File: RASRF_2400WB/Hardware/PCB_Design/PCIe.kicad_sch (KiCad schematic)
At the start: 1 part, among them J1 PCIexpress_x8

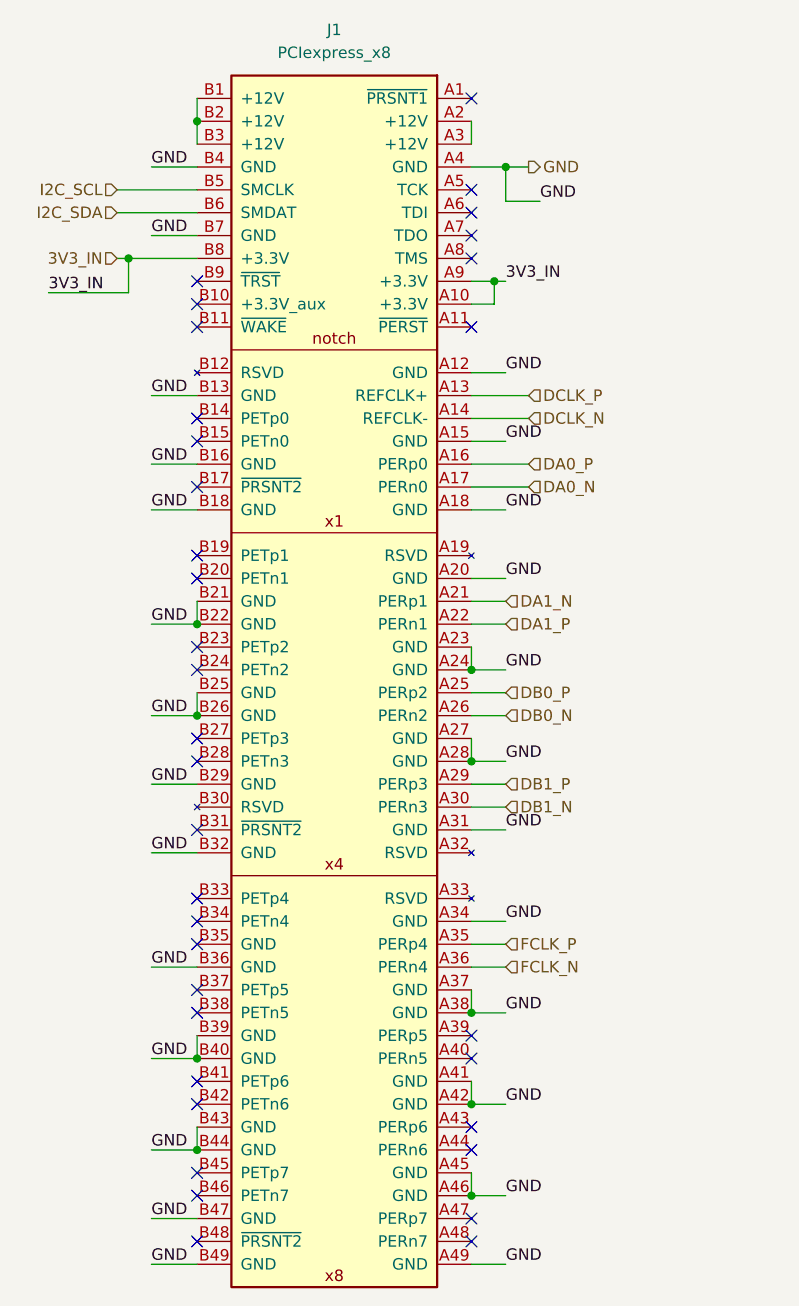
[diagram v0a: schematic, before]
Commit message: Corrected the RASRF_2400WB PCB design files. They where not the latest from Rev. A. sent to manufacturer.
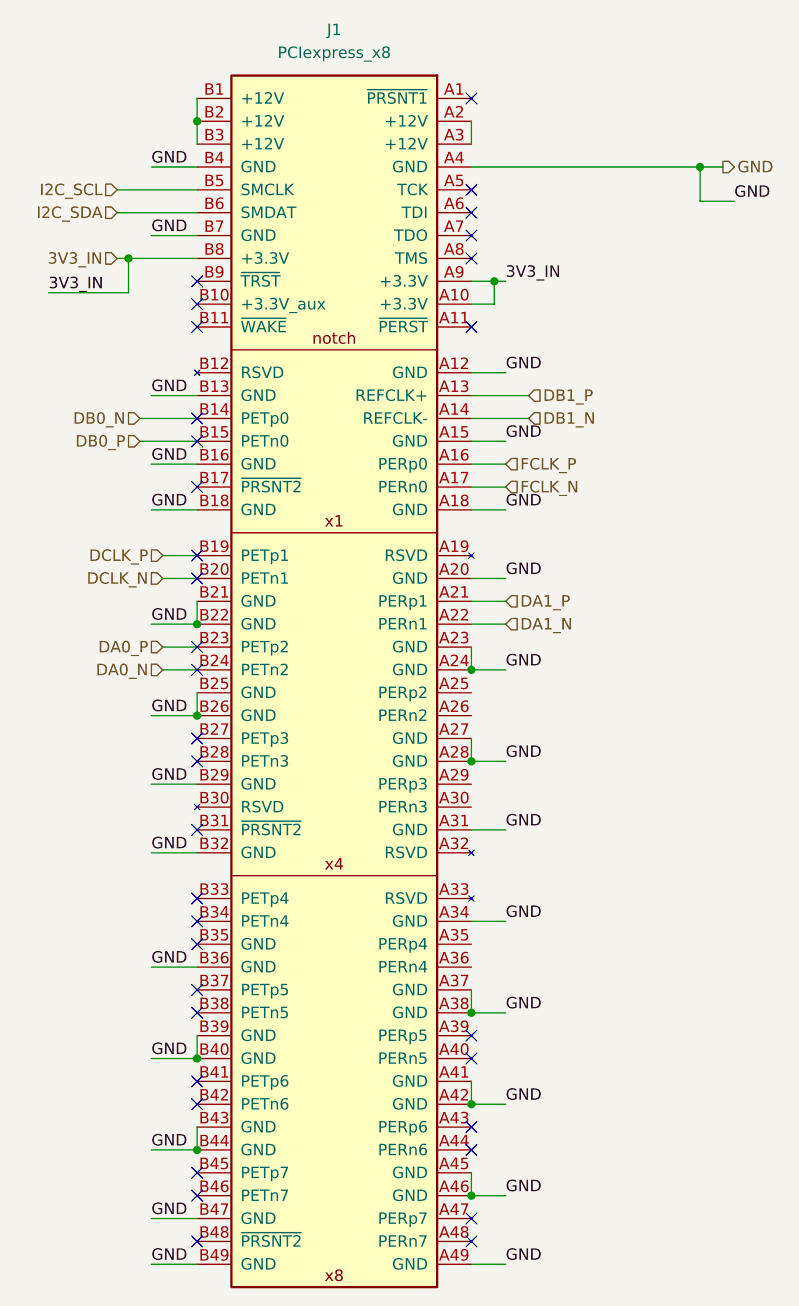
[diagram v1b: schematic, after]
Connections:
- net DA0_N: now also J1.B24 (PETn2); no longer J1.A17 (PERn0)
- net DA0_P: now also J1.B23 (PETp2); no longer J1.A16 (PERp0)
- net DA1_N: now also J1.A22 (PERn1); no longer J1.A21 (PERp1)
- net DA1_P: now also J1.A21 (PERp1); no longer J1.A22 (PERn1)
- net DB0_N: now also J1.B14 (PETp0); no longer J1.A26 (PERn2)
- net DB0_P: now also J1.B15 (PETn0); no longer J1.A25 (PERp2)
- net DB1_N: now also J1.A14 (REFCLK-); no longer J1.A30 (PERn3)
- net DB1_P: now also J1.A13 (REFCLK+); no longer J1.A29 (PERp3)
- net DCLK_N: now also J1.B20 (PETn1); no longer J1.A14 (REFCLK-)
- net DCLK_P: now also J1.B19 (PETp1); no longer J1.A13 (REFCLK+)
- net FCLK_N: now also J1.A17 (PERn0); no longer J1.A36 (PERn4)
- net FCLK_P: now also J1.A16 (PERp0); no longer J1.A35 (PERp4)
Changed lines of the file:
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@@
 	)
 	(junction
-		(at 106.68 45.72)
+		(at 128.27 45.72)
 		(diameter 0)
 		(color 0 0 0 0)
@@
 	(wire
 		(pts
-			(xy 106.68 134.62) (xy 102.87 134.62)
-		)
-		(stroke
-			(width 0)
-			(type default)
-		)
-	)
-	(wire
-		(pts
-			(xy 106.68 114.3) (xy 102.87 114.3)
+			(xy 102.87 45.72) (xy 128.27 45.72)
 		)
 		(stroke
@@
 	(wire
 		(pts
-			(xy 102.87 81.28) (xy 109.22 81.28)
-		)
-		(stroke
-			(width 0)
-			(type default)
-		)
-	)
-	(wire
-		(pts
 			(xy 67.31 71.12) (xy 72.39 71.12)
 		)
@@
 	(wire
 		(pts
-			(xy 110.49 49.53) (xy 106.68 49.53)
-		)
-		(stroke
-			(width 0)
-			(type default)
-		)
-	)
-	(wire
-		(pts
-			(xy 106.68 49.53) (xy 106.68 45.72)
+			(xy 132.08 49.53) (xy 128.27 49.53)
+		)
+		(stroke
+			(width 0)
+			(type default)
+		)
+	)
+	(wire
+		(pts
+			(xy 128.27 49.53) (xy 128.27 45.72)
 		)
 		(stroke
@@
 	(wire
 		(pts
-			(xy 106.68 132.08) (xy 102.87 132.08)
+			(xy 106.68 81.28) (xy 102.87 81.28)
 		)
 		(stroke
@@
 	(wire
 		(pts
+			(xy 68.58 91.44) (xy 72.39 91.44)
+		)
+		(stroke
+			(width 0)
+			(type default)
+		)
+	)
+	(wire
+		(pts
 			(xy 102.87 149.86) (xy 106.68 149.86)
 		)
@@
 	(wire
 		(pts
-			(xy 106.68 104.14) (xy 102.87 104.14)
+			(xy 68.58 88.9) (xy 72.39 88.9)
 		)
 		(stroke
@@
 	(wire
 		(pts
+			(xy 68.58 99.06) (xy 72.39 99.06)
+		)
+		(stroke
+			(width 0)
+			(type default)
+		)
+	)
+	(wire
+		(pts
 			(xy 102.87 157.48) (xy 102.87 160.02)
 		)
@@
 	(wire
 		(pts
+			(xy 106.68 78.74) (xy 102.87 78.74)
+		)
+		(stroke
+			(width 0)
+			(type default)
+		)
+	)
+	(wire
+		(pts
 			(xy 102.87 76.2) (xy 106.68 76.2)
 		)
@@
 	(wire
 		(pts
+			(xy 72.39 76.2) (xy 66.04 76.2)
+		)
+		(stroke
+			(width 0)
+			(type default)
+		)
+	)
+	(wire
+		(pts
+			(xy 68.58 101.6) (xy 72.39 101.6)
+		)
+		(stroke
+			(width 0)
+			(type default)
+		)
+	)
+	(wire
+		(pts
 			(xy 109.22 73.66) (xy 102.87 73.66)
 		)
@@
 	(wire
 		(pts
-			(xy 106.68 106.68) (xy 102.87 106.68)
-		)
-		(stroke
-			(width 0)
-			(type default)
-		)
-	)
-	(wire
-		(pts
 			(xy 67.31 162.56) (xy 72.39 162.56)
 		)
@@
 	(wire
 		(pts
-			(xy 106.68 116.84) (xy 102.87 116.84)
-		)
-		(stroke
-			(width 0)
-			(type default)
-		)
-	)
-	(wire
-		(pts
-			(xy 102.87 78.74) (xy 109.22 78.74)
-		)
-		(stroke
-			(width 0)
-			(type default)
-		)
-	)
-	(wire
-		(pts
 			(xy 102.87 71.12) (xy 109.22 71.12)
 		)
@@
 	(wire
 		(pts
+			(xy 72.39 73.66) (xy 66.04 73.66)
+		)
+		(stroke
+			(width 0)
+			(type default)
+		)
+	)
+	(wire
+		(pts
 			(xy 106.68 93.98) (xy 102.87 93.98)
 		)
@@
 	(wire
 		(pts
-			(xy 109.22 45.72) (xy 106.68 45.72)
+			(xy 130.81 45.72) (xy 128.27 45.72)
 		)
 		(stroke
@@
 		(pts
 			(xy 67.31 114.3) (xy 72.39 114.3)
-		)
-		(stroke
-			(width 0)
-			(type default)
-		)
-	)
-	(wire
-		(pts
-			(xy 106.68 45.72) (xy 102.87 45.72)
 		)
 		(stroke
@@
 	)
 	(label "GND"
-		(at 110.49 49.53 0)
+		(at 132.08 49.53 0)
 		(effects
 			(font
@@
 		)
 	)
+	(hierarchical_label "DA1_P"
+		(shape input)
+		(at 106.68 93.98 0)
+		(effects
+			(font
+				(size 1.27 1.27)
+			)
+			(justify left)
+		)
+	)
+	(hierarchical_label "DB0_P"
+		(shape input)
+		(at 66.04 76.2 180)
+		(effects
+			(font
+				(size 1.27 1.27)
+			)
+			(justify right)
+		)
+	)
+	(hierarchical_label "DB1_P"
+		(shape input)
+		(at 109.22 71.12 0)
+		(effects
+			(font
+				(size 1.27 1.27)
+			)
+			(justify left)
+		)
+	)
+	(hierarchical_label "FCLK_N"
+		(shape input)
+		(at 106.68 81.28 0)
+		(effects
+			(font
+				(size 1.27 1.27)
+			)
+			(justify left)
+		)
+	)
+	(hierarchical_label "FCLK_P"
+		(shape input)
+		(at 106.68 78.74 0)
+		(effects
+			(font
+				(size 1.27 1.27)
+			)
+			(justify left)
+		)
+	)
 	(hierarchical_label "DA1_N"
-		(shape input)
-		(at 106.68 93.98 0)
-		(effects
-			(font
-				(size 1.27 1.27)
-			)
-			(justify left)
-		)
-	)
-	(hierarchical_label "FCLK_P"
-		(shape input)
-		(at 106.68 132.08 0)
-		(effects
-			(font
-				(size 1.27 1.27)
-			)
-			(justify left)
-		)
-	)
-	(hierarchical_label "DB0_N"
-		(shape input)
-		(at 106.68 106.68 0)
-		(effects
-			(font
-				(size 1.27 1.27)
-			)
-			(justify left)
-		)
-	)
-	(hierarchical_label "DCLK_P"
-		(shape input)
-		(at 109.22 71.12 0)
-		(effects
-			(font
-				(size 1.27 1.27)
-			)
-			(justify left)
-		)
-	)
-	(hierarchical_label "DB1_N"
-		(shape input)
-		(at 106.68 116.84 0)
-		(effects
-			(font
-				(size 1.27 1.27)
-			)
-			(justify left)
-		)
-	)
-	(hierarchical_label "DA1_P"
 		(shape input)
 		(at 106.68 96.52 0)
@@
 	(hierarchical_label "GND"
 		(shape output)
-		(at 109.22 45.72 0)
+		(at 130.81 45.72 0)
 		(effects
 			(font
@@
 	(hierarchical_label "DA0_N"
 		(shape input)
-		(at 109.22 81.28 0)
+		(at 68.58 101.6 180)
+		(effects
+			(font
+				(size 1.27 1.27)
+			)
+			(justify right)
+		)
+	)
+	(hierarchical_label "DCLK_N"
+		(shape input)
+		(at 68.58 91.44 180)
+		(effects
+			(font
+				(size 1.27 1.27)
+			)
+			(justify right)
+		)
+	)
+	(hierarchical_label "DB1_N"
+		(shape input)
+		(at 109.22 73.66 0)
 		(effects
 			(font
@@
 		)
 	)
-	(hierarchical_label "DCLK_N"
-		(shape input)
-		(at 109.22 73.66 0)
-		(effects
-			(font
-				(size 1.27 1.27)
-			)
-			(justify left)
+	(hierarchical_label "DA0_P"
+		(shape input)
+		(at 68.58 99.06 180)
+		(effects
+			(font
+				(size 1.27 1.27)
+			)
+			(justify right)
 		)
 	)
@@
 		)
 	)
-	(hierarchical_label "DB0_P"
-		(shape input)
-		(at 106.68 104.14 0)
-		(effects
-			(font
-				(size 1.27 1.27)
-			)
-			(justify left)
+	(hierarchical_label "DB0_N"
+		(shape input)
+		(at 66.04 73.66 180)
+		(effects
+			(font
+				(size 1.27 1.27)
+			)
+			(justify right)
 		)
 	)
@@
 		)
 	)
-	(hierarchical_label "DA0_P"
-		(shape input)
-		(at 109.22 78.74 0)
-		(effects
-			(font
-				(size 1.27 1.27)
-			)
-			(justify left)
+	(hierarchical_label "DCLK_P"
+		(shape input)
+		(at 68.58 88.9 180)
+		(effects
+			(font
+				(size 1.27 1.27)
+			)
+			(justify right)
 		)
 	)
@@
 		)
 	)
-	(hierarchical_label "DB1_P"
-		(shape input)
-		(at 106.68 114.3 0)
-		(effects
-			(font
-				(size 1.27 1.27)
-			)
-			(justify left)
-		)
-	)
-	(hierarchical_label "FCLK_N"
-		(shape input)
-		(at 106.68 134.62 0)
-		(effects
-			(font
-				(size 1.27 1.27)
-			)
-			(justify left)
-		)
-	)
